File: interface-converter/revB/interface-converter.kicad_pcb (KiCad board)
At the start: 2 copper layers, 38.7 x 31.2 mm, 47 parts, among them P1 USB_OTG, P10 TST, P11 TST, P12 TST, P13 TST, P2 Mezzanine-Receptacle, P3 Mezzanine-Header, P4 CONN_01X01, P5 CONN_01X01, P6 CONN_01X01, P7 CONN_01X01, P8 TST, P9 TST, U1 93LCxxB-6, U2 Osc, U3 FT232H

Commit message: Added robosub logo
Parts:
- added G***: LOGO, robosub_footprints:robosub_logo-medium, F.Cu at (126.0, 117.5)

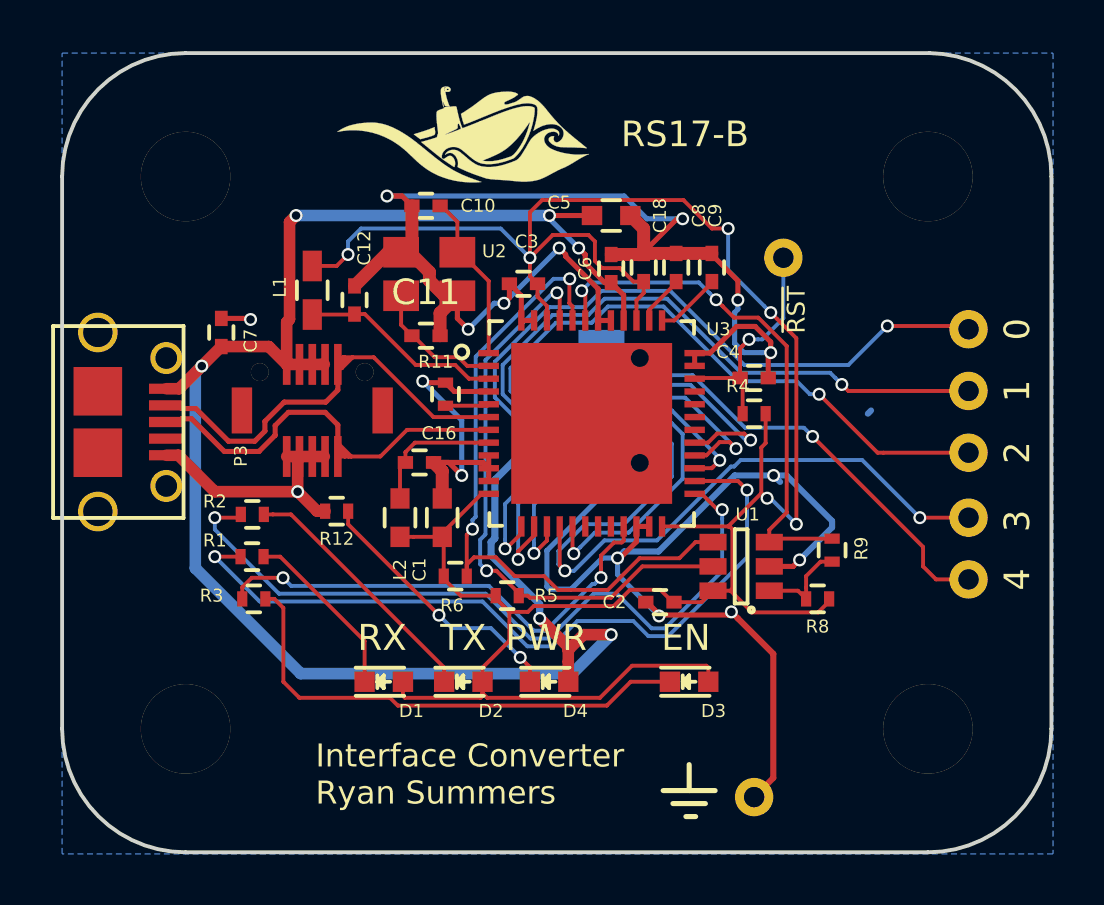
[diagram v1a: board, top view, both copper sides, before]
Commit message: Correction to interface board schematic
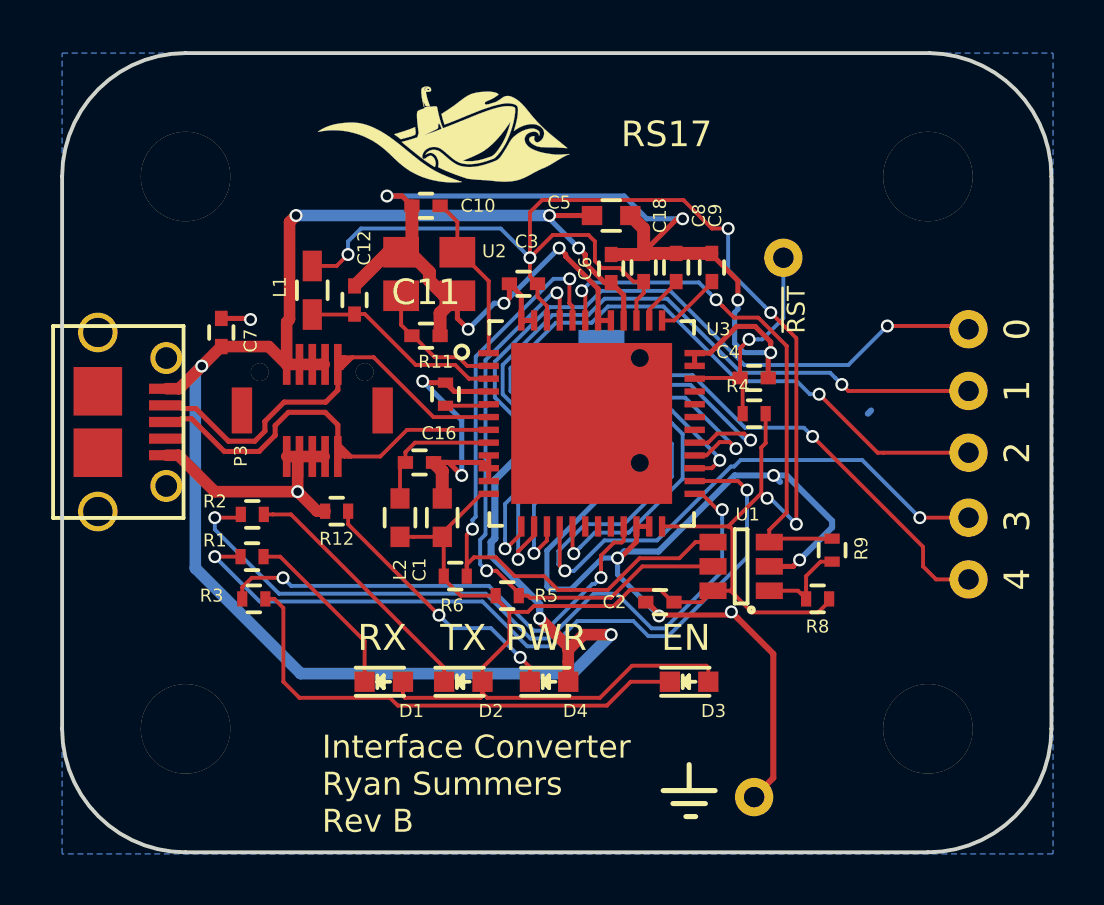
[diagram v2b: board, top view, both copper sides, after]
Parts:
- P2: footprint robosub_footprints:3mm-10pos-outer-outer-shroud -> robosub_footprints:3mm-10pos-outer-shroud
- moved G*** 0.76 mm to (125.2, 117.5)
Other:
- board text added: "Interface Converter Ryan Summers Rev B"
- board text added: "RS17"
- board text removed: "Interface Converter Ryan Summers"
- board text removed: "RS17-B"
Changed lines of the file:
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@@
       (net 27 /~RST))
-  )
-  (module robosub_footprints:3mm-10pos-outer-outer-shroud (layer B.Cu)
-    (at 131.318 128.143 90)
-    (attr smd)
-    (fp_text reference P2 (at 2.667 -1.778 180) (layer B.SilkS)
-      (effects (font (size 0.5 0.5) (thickness 0.075)) (justify mirror))
-    )
-    (fp_text value Mezzanine-Receptacle (at -1.778 -5.08 90) (layer B.Fab)
-      (effects (font (size 1 1) (thickness 0.15)) (justify mirror))
-    )
-    (pad "" thru_hole circle (at 2.05 1.5 90) (size 0.7 0.7) (drill 0.7) (layers *.Cu *.Mask))
-    (pad "" thru_hole circle (at -2.05 1.5 90) (size 0.7 0.7) (drill 0.7) (layers *.Cu *.Mask))
-    (pad 5 smd rect (at 0 -1.8 90) (size 0.3 1.6) (layers B.Cu B.Paste B.Mask)
-      (net 24 /AD1))
-    (pad 9 smd rect (at 1 -1.8 90) (size 0.3 1.6) (layers B.Cu B.Paste B.Mask)
-      (net 2 GND))
-    (pad 7 smd rect (at 0.5 -1.8 90) (size 0.3 1.6) (layers B.Cu B.Paste B.Mask)
-      (net 15 /AD2))
-    (pad 1 smd rect (at -1 -1.8 90) (size 0.3 1.6) (layers B.Cu B.Paste B.Mask)
-      (net 3 /Vbus))
-    (pad 3 smd rect (at -0.5 -1.8 90) (size 0.3 1.6) (layers B.Cu B.Paste B.Mask)
-      (net 14 /AD0))
-    (pad 6 smd rect (at 0 1.8 90) (size 0.3 1.6) (layers B.Cu B.Paste B.Mask)
-      (net 17 /AC3))
-    (pad 4 smd rect (at -0.5 1.8 90) (size 0.3 1.6) (layers B.Cu B.Paste B.Mask)
-      (net 16 /AD4))
-    (pad 2 smd rect (at -1 1.8 90) (size 0.3 1.6) (layers B.Cu B.Paste B.Mask)
-      (net 13 /AD3))
-    (pad 10 smd rect (at 1 1.8 90) (size 0.3 1.6) (layers B.Cu B.Paste B.Mask)
-      (net 19 /AC5))
-    (pad 8 smd rect (at 0.5 1.8 90) (size 0.3 1.6) (layers B.Cu B.Paste B.Mask)
-      (net 18 /AC4))
-    (pad "" smd rect (at 2.75 0 90) (size 0.8 1.8) (layers B.Cu B.Paste B.Mask))
-    (pad "" smd rect (at -2.75 0 90) (size 0.8 1.8) (layers B.Cu B.Paste B.Mask))
-    (model /home/ryan/repositories/pcbs/lib/3d-parts/3mm-10pos-outer-shroud.wrl
-      (at (xyz 0 0 0))
-      (scale (xyz 0.4 0.4 0.4))
-      (rotate (xyz -90 0 0))
-    )
   )
   (module robosub_footprints:3mm-10pos-outer-receptacle (layer F.Cu)
@@
     )
   )
+  (module robosub_footprints:3mm-10pos-outer-shroud (layer B.Cu)
+    (at 131.318 128.143 90)
+    (attr smd)
+    (fp_text reference P2 (at -2.794 -1.778 360) (layer B.SilkS)
+      (effects (font (size 0.5 0.5) (thickness 0.075)) (justify mirror))
+    )
+    (fp_text value Mezzanine-Receptacle (at -0.762 -3.81 90) (layer B.Fab)
+      (effects (font (size 1 1) (thickness 0.15)) (justify mirror))
+    )
+    (fp_line (start -2.35 1.9) (end 2.35 1.9) (layer B.SilkS) (width 0.15))
+    (fp_line (start -2.35 -1.9) (end 2.35 -1.9) (layer B.SilkS) (width 0.15))
+    (fp_line (start 2.35 1.9) (end 2.35 -1.9) (layer B.SilkS) (width 0.15))
+    (fp_line (start -2.35 1.9) (end -2.35 -1.9) (layer B.SilkS) (width 0.15))
+    (pad "" thru_hole circle (at 2.05 1.5 90) (size 0.7 0.7) (drill 0.7) (layers *.Cu *.Mask))
+    (pad "" thru_hole circle (at -2.05 1.5 90) (size 0.7 0.7) (drill 0.7) (layers *.Cu *.Mask))
+    (pad 5 smd rect (at 0 -1.8 90) (size 0.3 1.6) (layers B.Cu B.Paste B.Mask)
+      (net 24 /AD1))
+    (pad 9 smd rect (at 1 -1.8 90) (size 0.3 1.6) (layers B.Cu B.Paste B.Mask)
+      (net 2 GND))
+    (pad 7 smd rect (at 0.5 -1.8 90) (size 0.3 1.6) (layers B.Cu B.Paste B.Mask)
+      (net 15 /AD2))
+    (pad 1 smd rect (at -1 -1.8 90) (size 0.3 1.6) (layers B.Cu B.Paste B.Mask)
+      (net 3 /Vbus))
+    (pad 3 smd rect (at -0.5 -1.8 90) (size 0.3 1.6) (layers B.Cu B.Paste B.Mask)
+      (net 14 /AD0))
+    (pad 6 smd rect (at 0 1.8 90) (size 0.3 1.6) (layers B.Cu B.Paste B.Mask)
+      (net 17 /AC3))
+    (pad 4 smd rect (at -0.5 1.8 90) (size 0.3 1.6) (layers B.Cu B.Paste B.Mask)
+      (net 16 /AD4))
+    (pad 2 smd rect (at -1 1.8 90) (size 0.3 1.6) (layers B.Cu B.Paste B.Mask)
+      (net 13 /AD3))
+    (pad 10 smd rect (at 1 1.8 90) (size 0.3 1.6) (layers B.Cu B.Paste B.Mask)
+      (net 19 /AC5))
+    (pad 8 smd rect (at 0.5 1.8 90) (size 0.3 1.6) (layers B.Cu B.Paste B.Mask)
+      (net 18 /AC4))
+    (pad "" smd rect (at 2.75 0 90) (size 0.8 1.8) (layers B.Cu B.Paste B.Mask))
+    (pad "" smd rect (at -2.75 0 90) (size 0.8 1.8) (layers B.Cu B.Paste B.Mask))
+    (model robosub.3dshapes/3mm-10pos-outer-shroud.wrl
+      (at (xyz 0 0 0))
+      (scale (xyz 0.4 0.4 0.4))
+      (rotate (xyz -90 0 0))
+    )
+  )
   (module robosub_footprints:robosub_logo-medium (layer F.Cu)
-    (at 125.984 117.475)
+    (at 125.222 117.475)
     (fp_text reference G*** (at 0 0) (layer F.SilkS) hide
       (effects (font (thickness 0.3)))
@@
   (gr_line (start 135.382 143.51) (end 134.112 143.51) (layer F.SilkS) (width 0.2))
   (gr_line (start 133.731 143.002) (end 135.763 143.002) (layer F.SilkS) (width 0.2))
-  (gr_text RS17-B (at 132.08 117.348) (layer F.SilkS)
+  (gr_text RS17 (at 132.08 117.348) (layer F.SilkS)
     (effects (font (size 1 1) (thickness 0.2)) (justify left))
   )
-  (gr_text "Interface Converter\nRyan Summers" (at 120.142 142.367) (layer F.SilkS)
+  (gr_text "Interface Converter\nRyan Summers\nRev B" (at 120.396 142.748) (layer F.SilkS)
     (effects (font (size 0.9 0.9) (thickness 0.18)) (justify left))
   )
